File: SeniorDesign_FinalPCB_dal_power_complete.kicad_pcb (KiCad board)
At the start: 2 copper layers, 172.7 x 167.4 mm, 226 parts, among them J1 5000, J10 5000, J11 POWER, J2 5000, J3 5000, J4 5000, J5 5000, J6 5000, J7 5000, J8 5000, J9 5000, Q1 Si7450DP, Q10 Si7450DP, Q11 Si7450DP, Q12 Si7450DP, Q13 Si7450DP, Q14 Si7450DP, Q15 Si7450DP, Q16 Si7450DP, Q2 Si7450DP, Q3 Si7450DP, Q4 Si7450DP, Q5 Si7450DP, Q6 Si7450DP, Q7 Si7450DP, Q8 Si7450DP, Q9 Si7450DP, U1 Transducer, U10 Transducer, U11 Transducer, U12 Transducer, U13 Transducer, U14 Transducer, U15 Transducer, U16 Transducer, U17 Transducer, U18 Transducer, U19 Transducer, U2 Transducer, U20 Transducer, U21 Transducer, U22 Transducer, U23 Transducer, U24 Transducer, U25 Transducer, U26 Transducer, U27 Transducer, U28 Transducer, U29 Transducer, U3 Transducer, U30 Transducer, U31 Transducer, U32 Transducer, U33 Transducer, U34 Transducer, U35 Transducer, U36 Transducer, U37 Transducer, U38 Transducer, U39 Transducer, U4 Transducer, U40 Transducer, U41 Transducer, U42 Transducer, U43 Transducer, U44 Transducer, U45 Transducer, U46 Transducer, U47 Transducer, U48 Transducer, U49 Transducer, U5 Transducer, U50 Transducer, U51 Transducer, U52 Transducer, U53 Transducer, U54 Transducer, U55 Transducer, U56 Transducer, U57 Transducer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

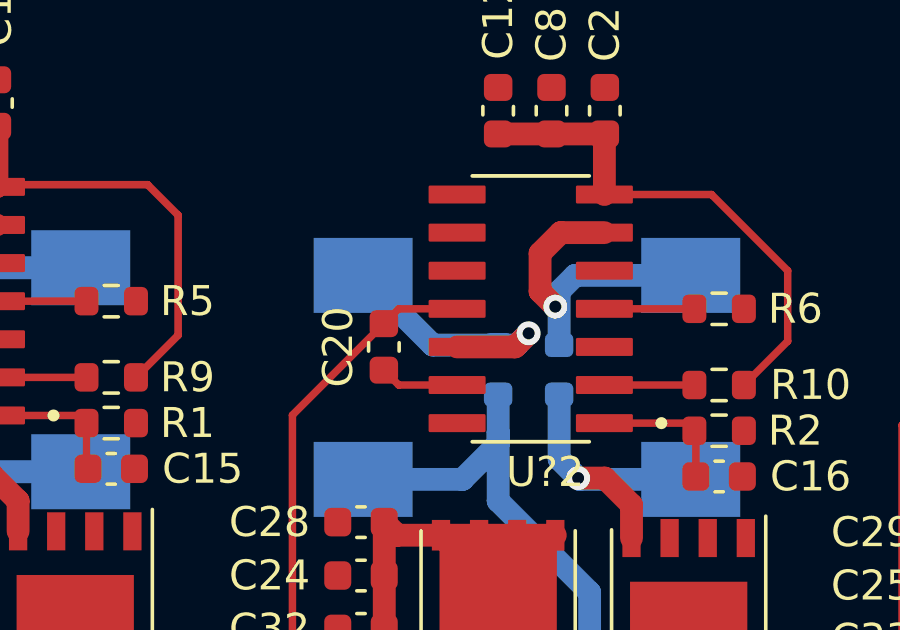
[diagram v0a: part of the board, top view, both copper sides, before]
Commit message: Fixed a via DRC error
dan messed up :o
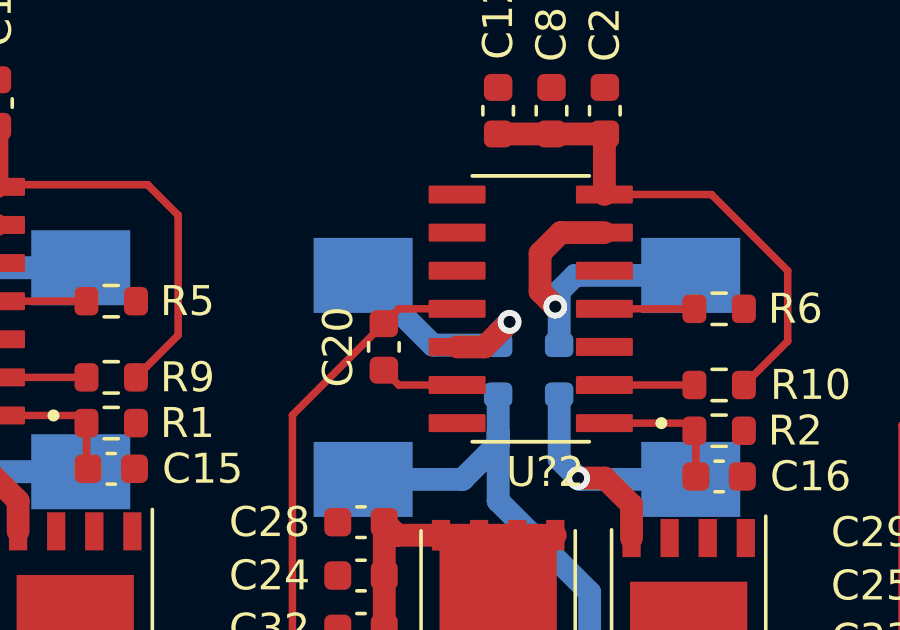
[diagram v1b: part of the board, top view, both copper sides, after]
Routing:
- net Net-(D3-Pad1): track 9.71 -> 8.49 mm
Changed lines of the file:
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@@
   (segment (start 314.1275 31.6935) (end 315.367 30.454) (width 0.762) (layer "B.Cu") (net 32))
   (segment (start 315.367 30.454) (end 318.4455 30.454) (width 0.762) (layer "B.Cu") (net 32))
-  (segment (start 332.921 33.093) (end 333.375 32.639) (width 0.762) (layer "F.Cu") (net 33))
-  (segment (start 330.9905 33.093) (end 332.921 33.093) (width 0.762) (layer "F.Cu") (net 33))
-  (via (at 333.375 32.639) (size 0.8) (drill 0.4) (layers "F.Cu" "B.Cu") (net 33))
-  (segment (start 327.8575 31.1315) (end 327.8575 30.709) (width 0.25) (layer "B.Cu") (net 33))
-  (segment (start 332.359 33.03) (end 332.984 33.03) (width 0.762) (layer "B.Cu") (net 33))
+  (segment (start 330.9905 33.093) (end 331.905 33.093) (width 0.762) (layer "F.Cu") (net 33))
+  (segment (start 331.905 33.093) (end 332.74 32.258) (width 0.762) (layer "F.Cu") (net 33))
+  (via (at 332.74 32.258) (size 0.8) (drill 0.4) (layers "F.Cu" "B.Cu") (net 33))
   (segment (start 332.359 33.03) (end 330.1785 33.03) (width 0.762) (layer "B.Cu") (net 33))
-  (segment (start 333.33548 32.67852) (end 333.33548 32.639) (width 0.762) (layer "B.Cu") (net 33))
-  (segment (start 332.296 33.093) (end 332.359 33.03) (width 0.25) (layer "B.Cu") (net 33))
-  (segment (start 332.984 33.03) (end 333.33548 32.67852) (width 0.762) (layer "B.Cu") (net 33))
+  (segment (start 332.359 32.639) (end 332.74 32.258) (width 0.762) (layer "B.Cu") (net 33))
+  (segment (start 332.359 33.03) (end 332.359 32.639) (width 0.762) (layer "B.Cu") (net 33))
   (segment (start 330.1785 33.03) (end 327.8575 30.709) (width 0.762) (layer "B.Cu") (net 33))
   (segment (start 334.264 44.835) (end 334.587 44.835) (width 0.762) (layer "F.Cu") (net 34))

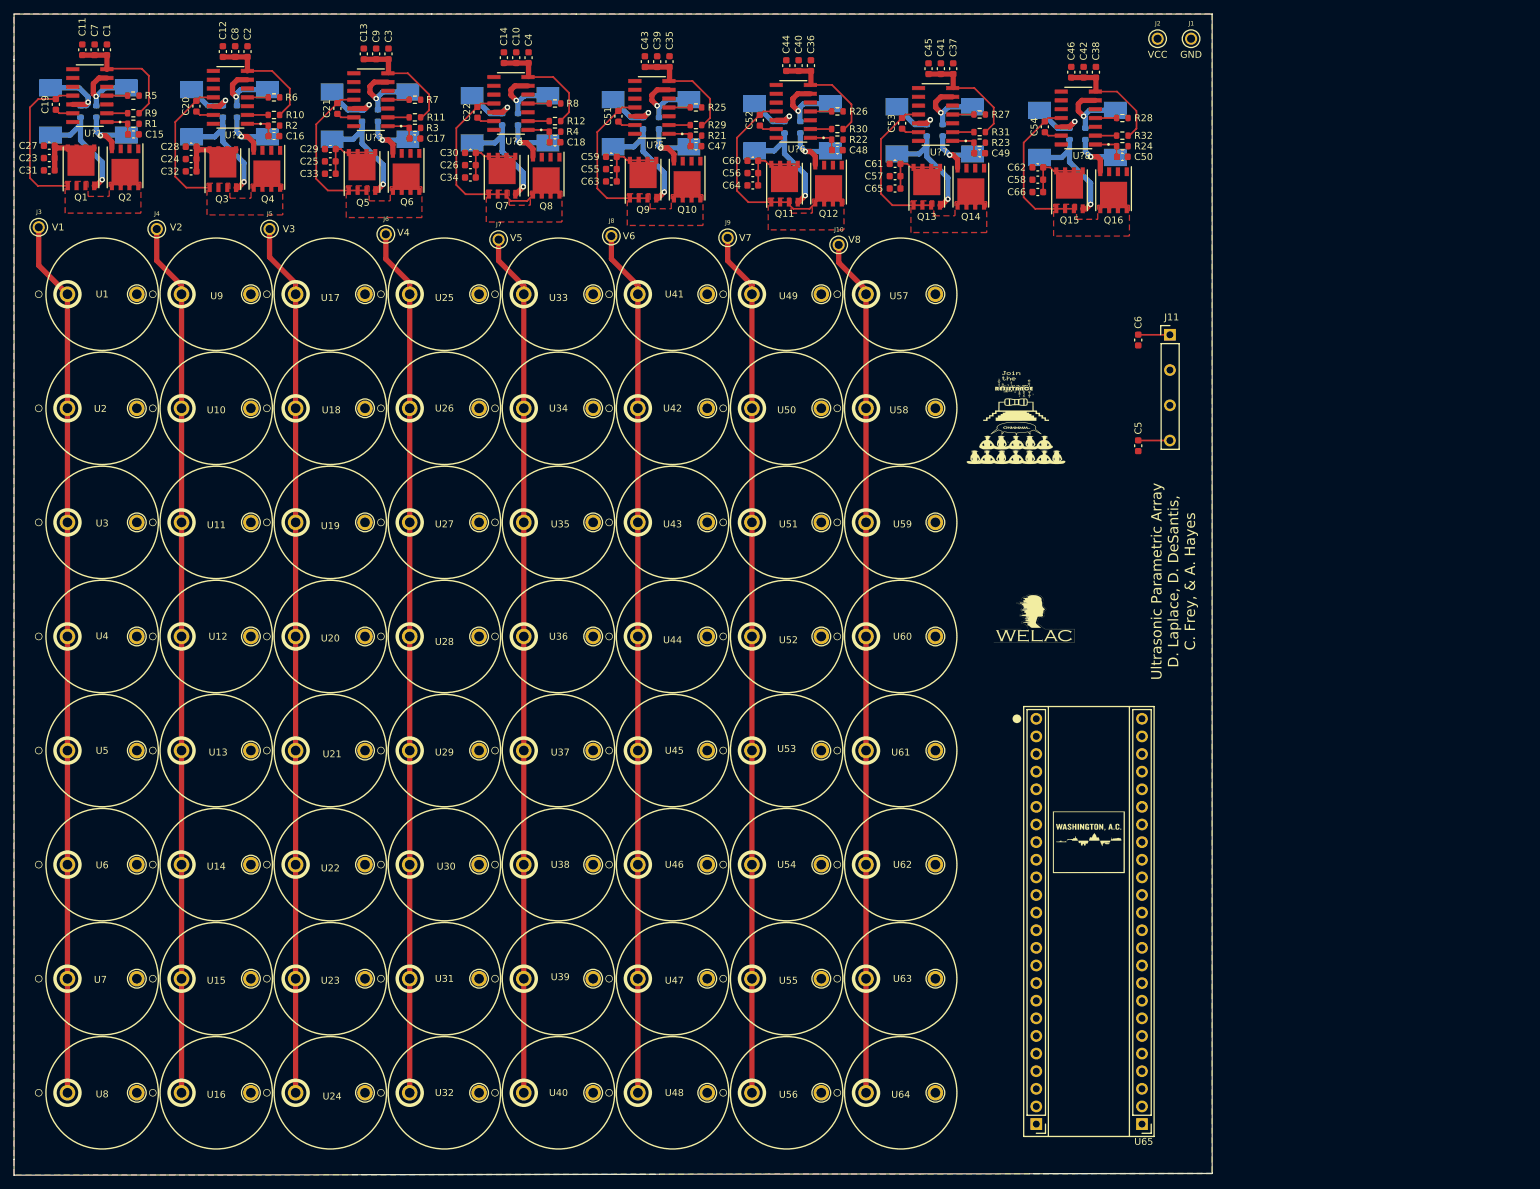
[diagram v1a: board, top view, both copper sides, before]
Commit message: all major components added, routing underway
added and fixed some component footprints. routed column signals and designed/layout of audio amplifier and power supply. NEED TO CHECK CAP VOLTAGES
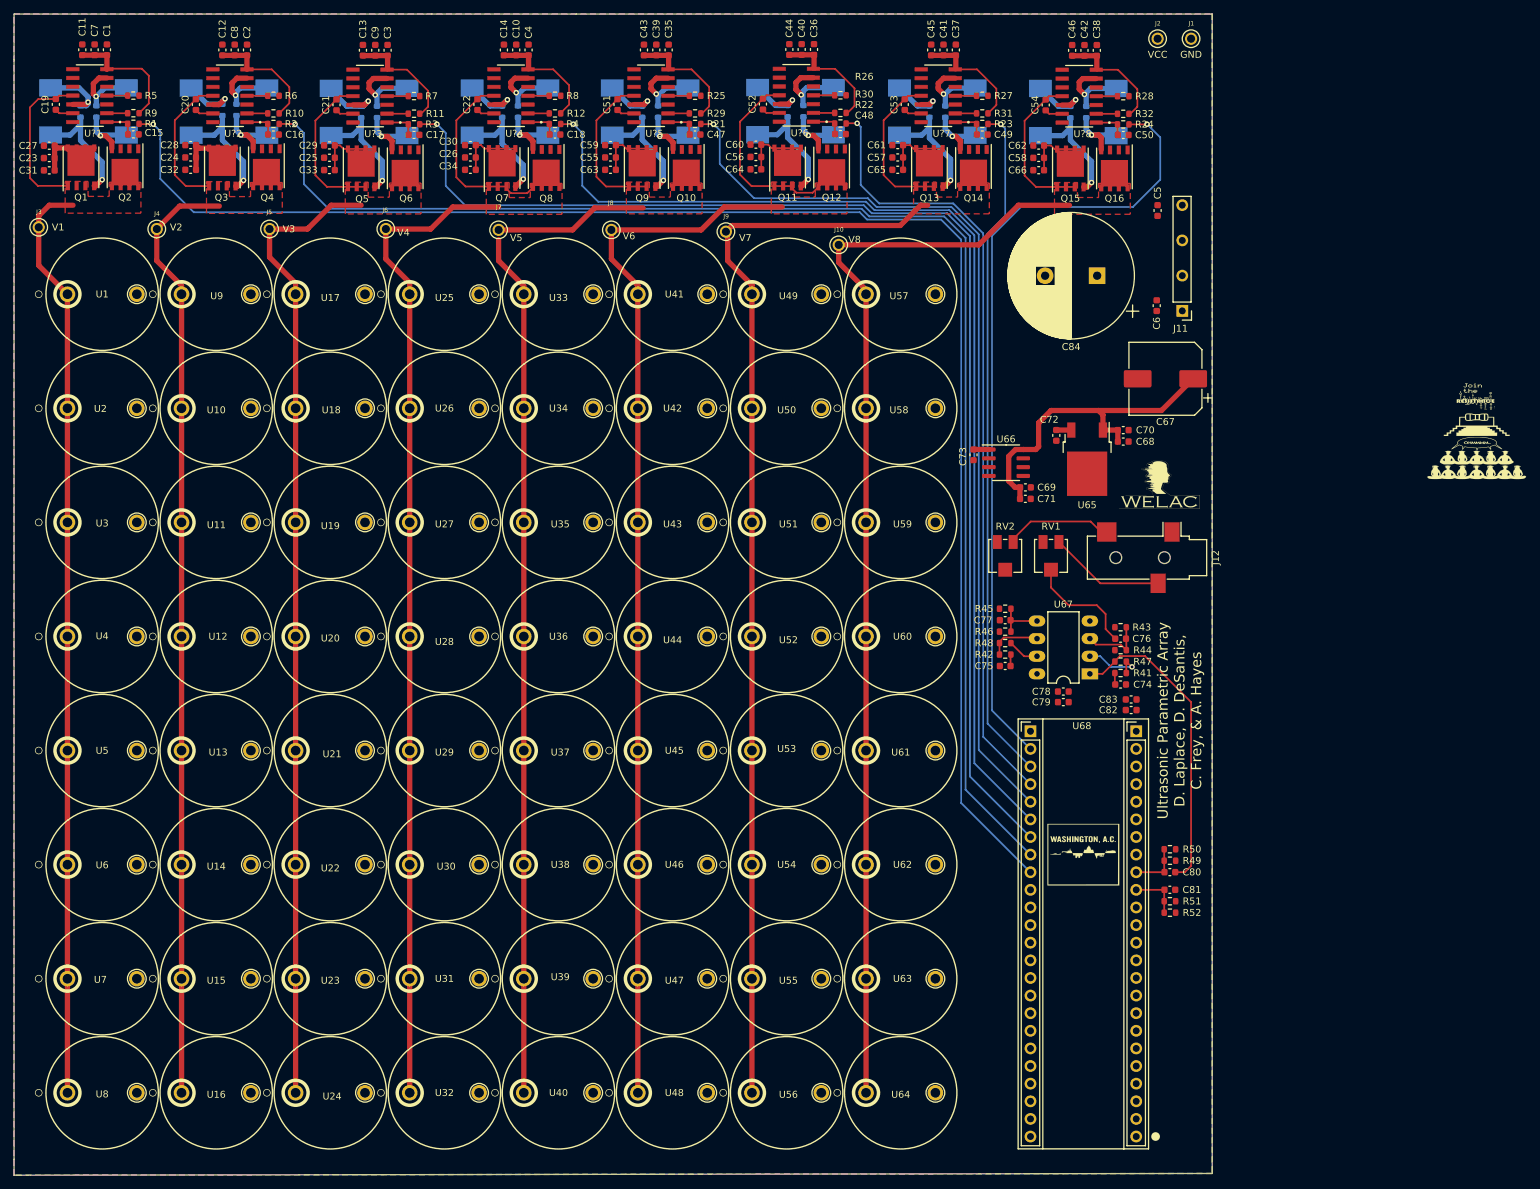
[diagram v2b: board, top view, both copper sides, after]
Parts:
- added C67: 470uF 25V, Capacitor_SMD:CP_Elec_10x10, F.Cu at (468.2, 72.4)
- added C68: 10u, Capacitor_SMD:C_0603_1608Metric, F.Cu at (462.2, 81.4)
- added C69: 10u, Capacitor_SMD:C_0603_1608Metric, F.Cu at (448.1, 88.0)
- added C70: 0.1u, Capacitor_SMD:C_0603_1608Metric, F.Cu at (462.2, 79.8)
- added C71: 0.1u, Capacitor_SMD:C_0603_1608Metric, F.Cu at (448.0, 89.7)
- added C72: 0.1u, Capacitor_SMD:C_0603_1608Metric, F.Cu at (452.5, 80.6)
- added C73: 0.1u, Capacitor_SMD:C_0603_1608Metric, F.Cu at (440.6, 83.3)
- added C74: 10u 10V, Capacitor_SMD:C_0603_1608Metric, F.Cu at (461.8, 116.5)
- added C75: 10u 10V, Capacitor_SMD:C_0603_1608Metric, F.Cu at (445.1, 113.8)
- added C76: 10uF 10V, Capacitor_SMD:C_0603_1608Metric, F.Cu at (461.8, 109.9)
- added C77: 10uF 10V, Capacitor_SMD:C_0603_1608Metric, F.Cu at (445.1, 107.2)
- added C78: 0.1uF, Capacitor_SMD:C_0603_1608Metric, F.Cu at (453.5, 117.5)
- added C79: 10uF 10V, Capacitor_SMD:C_0603_1608Metric, F.Cu at (453.5, 119.0)
- added C80: 10uF 10V, Capacitor_SMD:C_0603_1608Metric, F.Cu at (468.9, 143.5)
- added C81: 10uF 10V, Capacitor_SMD:C_0603_1608Metric, F.Cu at (468.9, 146.1)
- added C82: 10uF 10V, Capacitor_SMD:C_0603_1608Metric, F.Cu at (463.3, 120.1)
- added C83: 0.1uF, Capacitor_SMD:C_0603_1608Metric, F.Cu at (463.3, 118.6)
- added C84: 100u, Capacitor_THT:CP_Radial_D18.0mm_P7.50mm, F.Cu at (458.4, 57.5)
- added J12: AudioJack3, Connector_Audio:Jack_3.5mm_CUI_SJ-3523-SMT_Horizontal, F.Cu at (465.6, 98.2)
- added R41: 1k, Resistor_SMD:R_0603_1608Metric, F.Cu at (461.8, 114.8)
- added R42: 1k, Resistor_SMD:R_0603_1608Metric, F.Cu at (445.1, 112.1)
- added R43: 22k, Resistor_SMD:R_0603_1608Metric, F.Cu at (461.8, 108.2)
- added R44: 22k, Resistor_SMD:R_0603_1608Metric, F.Cu at (461.8, 111.5)
- added R45: 22k, Resistor_SMD:R_0603_1608Metric, F.Cu at (445.1, 105.5)
- added R46: 22k, Resistor_SMD:R_0603_1608Metric, F.Cu at (445.1, 108.8)
- added R47: 4.7k, Resistor_SMD:R_0603_1608Metric, F.Cu at (461.8, 113.2)
- added R48: 4.7k, Resistor_SMD:R_0603_1608Metric, F.Cu at (445.1, 110.5)
- added R49: 2k, Resistor_SMD:R_0603_1608Metric, F.Cu at (468.9, 141.9)
- added R50: 1k, Resistor_SMD:R_0603_1608Metric, F.Cu at (468.9, 140.2)
- added R51: 2k, Resistor_SMD:R_0603_1608Metric, F.Cu at (468.9, 147.7)
- added R52: 1k, Resistor_SMD:R_0603_1608Metric, F.Cu at (468.9, 149.4)
- added RV1: 1k, Potentiometer_SMD:Potentiometer_Bourns_3314J_Vertical, F.Cu at (451.7, 97.9)
- added RV2: 1k, Potentiometer_SMD:Potentiometer_Bourns_3314J_Vertical, F.Cu at (445.1, 97.9)
- added U66: LM78L05_SO8, Package_SO:SOIC-8_3.9x4.9mm_P1.27mm, F.Cu at (445.3, 84.5)
- added U67: TL082, Package_DIP:DIP-8_W7.62mm_LongPads, F.Cu at (457.3, 114.9)
- added U68: CMOD_A7, Senior:CMOD A7, F.Cu at (464.0, 123.2)
- U65: value CMOD_A7 -> LM78M05_TO252; footprint SeniorDesign:CMOD A7 -> Package_TO_SOT_SMD:TO-252-2
- moved U65 96.1 mm to (456.9, 84.0), turned to -90 degrees
- moved G*** 66.6 mm to (510.2, 77.1)
- moved G*** 66.4 mm to (513.2, 82.2)
- moved C5 34.0 mm to (467.1, 48.1)
- moved G*** 26.4 mm to (467.4, 87.9)
- moved C6 5.63 mm to (467.0, 61.8), turned to 90 degrees
- moved J11 3.88 mm to (470.7, 62.6), turned to 180 degrees
- moved C54 3.15 mm to (451.0, 32.9)
- moved C38 3.15 mm to (458.3, 25.1)
- moved C42 3.15 mm to (456.6, 25.1)
- moved C46 3.15 mm to (454.8, 25.1)
- moved C50 3.15 mm to (462.2, 37.2)
- moved C58 3.15 mm to (450.0, 40.5)
- moved C62 3.15 mm to (450.0, 38.8)
- moved C66 3.15 mm to (450.0, 42.3)
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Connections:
- C19 pad 1: /pwm_driver/COL1_OUT -> COL1_OUT
- C20 pad 1: /pwm_driver/COL2_OUT -> COL2_OUT
- C21 pad 1: /pwm_driver/COL3_OUT -> COL3_OUT
- C22 pad 1: /pwm_driver/COL4_OUT -> COL4_OUT
- C51 pad 1: /pwm_driver/COL5_OUT -> COL5_OUT
- C52 pad 1: /pwm_driver/COL6_OUT -> COL6_OUT
- C53 pad 1: /pwm_driver/COL7_OUT -> COL7_OUT
- C54 pad 1: /pwm_driver/COL8_OUT -> COL8_OUT
- Q1 pad 1: /pwm_driver/COL1_OUT -> COL1_OUT
- Q1 pad 2: /pwm_driver/COL1_OUT -> COL1_OUT
- Q1 pad 3: /pwm_driver/COL1_OUT -> COL1_OUT
- Q10 pad 5: /pwm_driver/COL5_OUT -> COL5_OUT
- Q11 pad 1: /pwm_driver/COL6_OUT -> COL6_OUT
- Q11 pad 2: /pwm_driver/COL6_OUT -> COL6_OUT
- Q11 pad 3: /pwm_driver/COL6_OUT -> COL6_OUT
- Q12 pad 5: /pwm_driver/COL6_OUT -> COL6_OUT
- Q13 pad 1: /pwm_driver/COL7_OUT -> COL7_OUT
- Q13 pad 2: /pwm_driver/COL7_OUT -> COL7_OUT
- Q13 pad 3: /pwm_driver/COL7_OUT -> COL7_OUT
- Q14 pad 5: /pwm_driver/COL7_OUT -> COL7_OUT
- Q15 pad 1: /pwm_driver/COL8_OUT -> COL8_OUT
- Q15 pad 2: /pwm_driver/COL8_OUT -> COL8_OUT
- Q15 pad 3: /pwm_driver/COL8_OUT -> COL8_OUT
- Q16 pad 5: /pwm_driver/COL8_OUT -> COL8_OUT
- Q2 pad 5: /pwm_driver/COL1_OUT -> COL1_OUT
- Q3 pad 1: /pwm_driver/COL2_OUT -> COL2_OUT
- Q3 pad 2: /pwm_driver/COL2_OUT -> COL2_OUT
- Q3 pad 3: /pwm_driver/COL2_OUT -> COL2_OUT
- Q4 pad 5: /pwm_driver/COL2_OUT -> COL2_OUT
- Q5 pad 1: /pwm_driver/COL3_OUT -> COL3_OUT
- Q5 pad 2: /pwm_driver/COL3_OUT -> COL3_OUT
- Q5 pad 3: /pwm_driver/COL3_OUT -> COL3_OUT
- Q6 pad 5: /pwm_driver/COL3_OUT -> COL3_OUT
- Q7 pad 1: /pwm_driver/COL4_OUT -> COL4_OUT
- Q7 pad 2: /pwm_driver/COL4_OUT -> COL4_OUT
- Q7 pad 3: /pwm_driver/COL4_OUT -> COL4_OUT
- Q8 pad 5: /pwm_driver/COL4_OUT -> COL4_OUT
- Q9 pad 1: /pwm_driver/COL5_OUT -> COL5_OUT
- Q9 pad 2: /pwm_driver/COL5_OUT -> COL5_OUT
- Q9 pad 3: /pwm_driver/COL5_OUT -> COL5_OUT
- R1 pad 2: /pwm_driver/COL1_SIG -> COL1_SIG
- R2 pad 2: /pwm_driver/COL2_SIG -> COL2_SIG
- R21 pad 2: /pwm_driver/COL5_SIG -> COL5_SIG
- R22 pad 2: /pwm_driver/COL6_SIG -> COL6_SIG
- R23 pad 2: /pwm_driver/COL7_SIG -> COL7_SIG
- R24 pad 2: /pwm_driver/COL8_SIG -> COL8_SIG
- R3 pad 2: /pwm_driver/COL3_SIG -> COL3_SIG
- R4 pad 2: /pwm_driver/COL4_SIG -> COL4_SIG
- U65 pad 1: unconnected-(U65-Pad1) -> +12V
- U65 pad 2: unconnected-(U65-Pad2) -> GND
- U65 pad 3: unconnected-(U65-Pad3) -> +5V
- U?1 pad 11: /pwm_driver/COL1_OUT -> COL1_OUT
- U?2 pad 11: /pwm_driver/COL2_OUT -> COL2_OUT
- U?3 pad 11: /pwm_driver/COL3_OUT -> COL3_OUT
- U?4 pad 11: /pwm_driver/COL4_OUT -> COL4_OUT
- U?5 pad 11: /pwm_driver/COL5_OUT -> COL5_OUT
- U?6 pad 11: /pwm_driver/COL6_OUT -> COL6_OUT
- U?7 pad 11: /pwm_driver/COL7_OUT -> COL7_OUT
- U?8 pad 11: /pwm_driver/COL8_OUT -> COL8_OUT
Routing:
- net COL1_SIG: track 0.00 -> 224.8 mm, vias 0 -> 1
- net COL2_SIG: track 0.00 -> 202.8 mm, vias 0 -> 1
- net COL3_SIG: track 0.00 -> 180.7 mm, vias 0 -> 1
- net COL4_SIG: track 0.00 -> 158.3 mm, vias 0 -> 1
- net COL5_SIG: track 0.00 -> 134.4 mm, vias 0 -> 1
- net COL8_SIG: track 0.00 -> 115.3 mm, vias 0 -> 1
- net COL6_SIG: track 0.00 -> 113.5 mm, vias 0 -> 1
- net COL7_SIG: track 0.00 -> 98.3 mm, vias 0 -> 1
- net COL8_OUT: track 124.0 -> 182.7 mm
- net COL6_OUT: track 125.1 -> 178.9 mm
- net COL7_OUT: track 124.8 -> 178.5 mm
- net COL5_OUT: track 124.6 -> 169.9 mm
- net COL4_OUT: track 125.3 -> 170.5 mm
- net Net-(C80-Pad1): track 0.00 -> 44.7 mm
- net +12V: track 141.1 -> 183.9 mm
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- added copper zone on F.Cu, net COL1_OUT
- added copper zone on F.Cu, net COL2_OUT
- added copper zone on F.Cu, net COL3_OUT
- added copper zone on F.Cu, net COL4_OUT
- added copper zone on F.Cu, net COL5_OUT
- added copper zone on F.Cu, net COL6_OUT
- added copper zone on F.Cu, net COL7_OUT
- added copper zone on F.Cu, net COL8_OUT
- removed copper zone on F.Cu, net /pwm_driver/COL1_OUT
- removed copper zone on F.Cu, net /pwm_driver/COL2_OUT
- removed copper zone on F.Cu, net /pwm_driver/COL3_OUT
- removed copper zone on F.Cu, net /pwm_driver/COL4_OUT
- removed copper zone on F.Cu, net /pwm_driver/COL5_OUT
- removed copper zone on F.Cu, net /pwm_driver/COL6_OUT
- removed copper zone on F.Cu, net /pwm_driver/COL7_OUT
- removed copper zone on F.Cu, net /pwm_driver/COL8_OUT
